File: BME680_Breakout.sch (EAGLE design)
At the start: 23 parts, among them U1 BME680, U4 PCA9515ADP, U8 LD1117XX

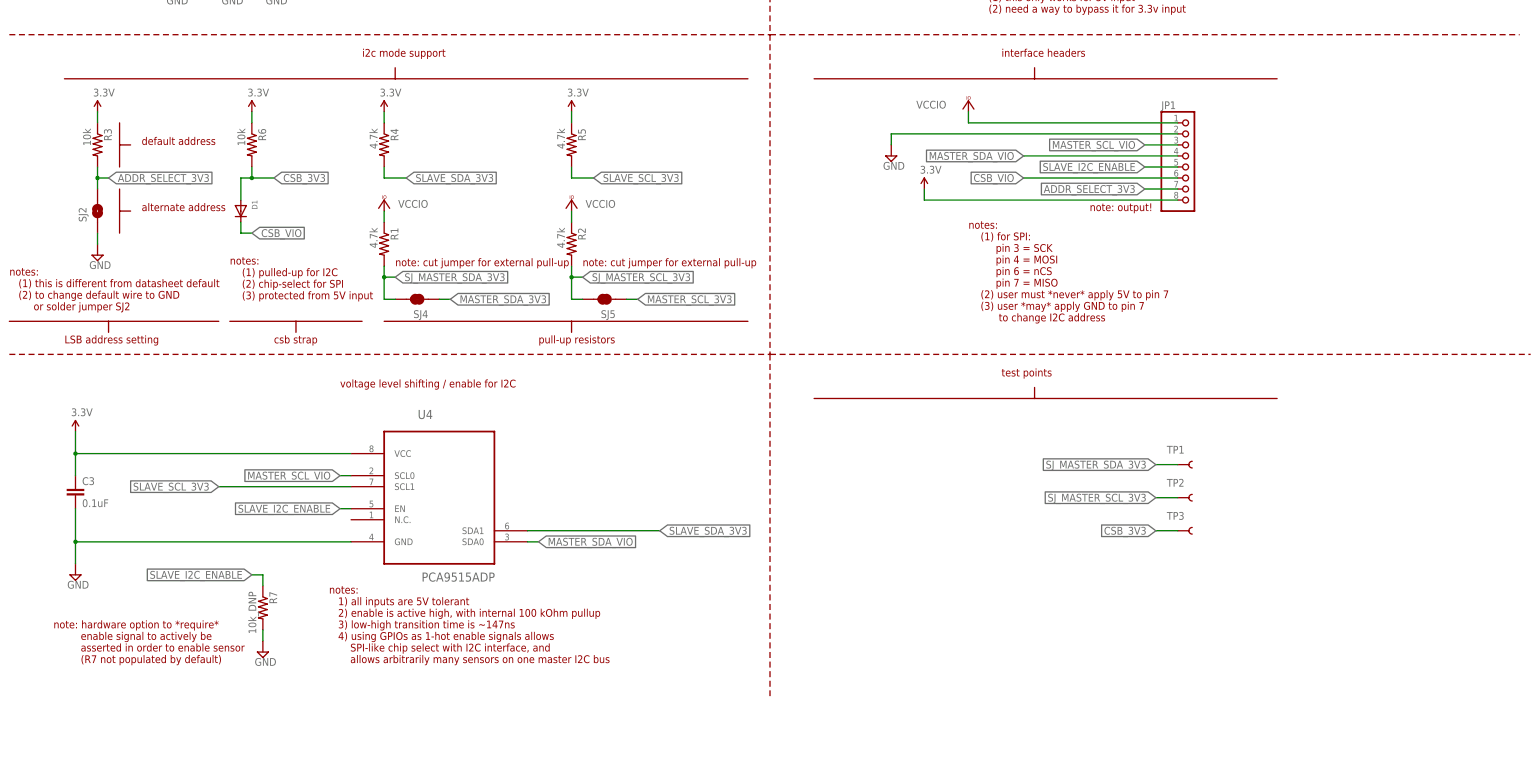
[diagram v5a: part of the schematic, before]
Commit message: asded zener diode and ptc fuse to address select input
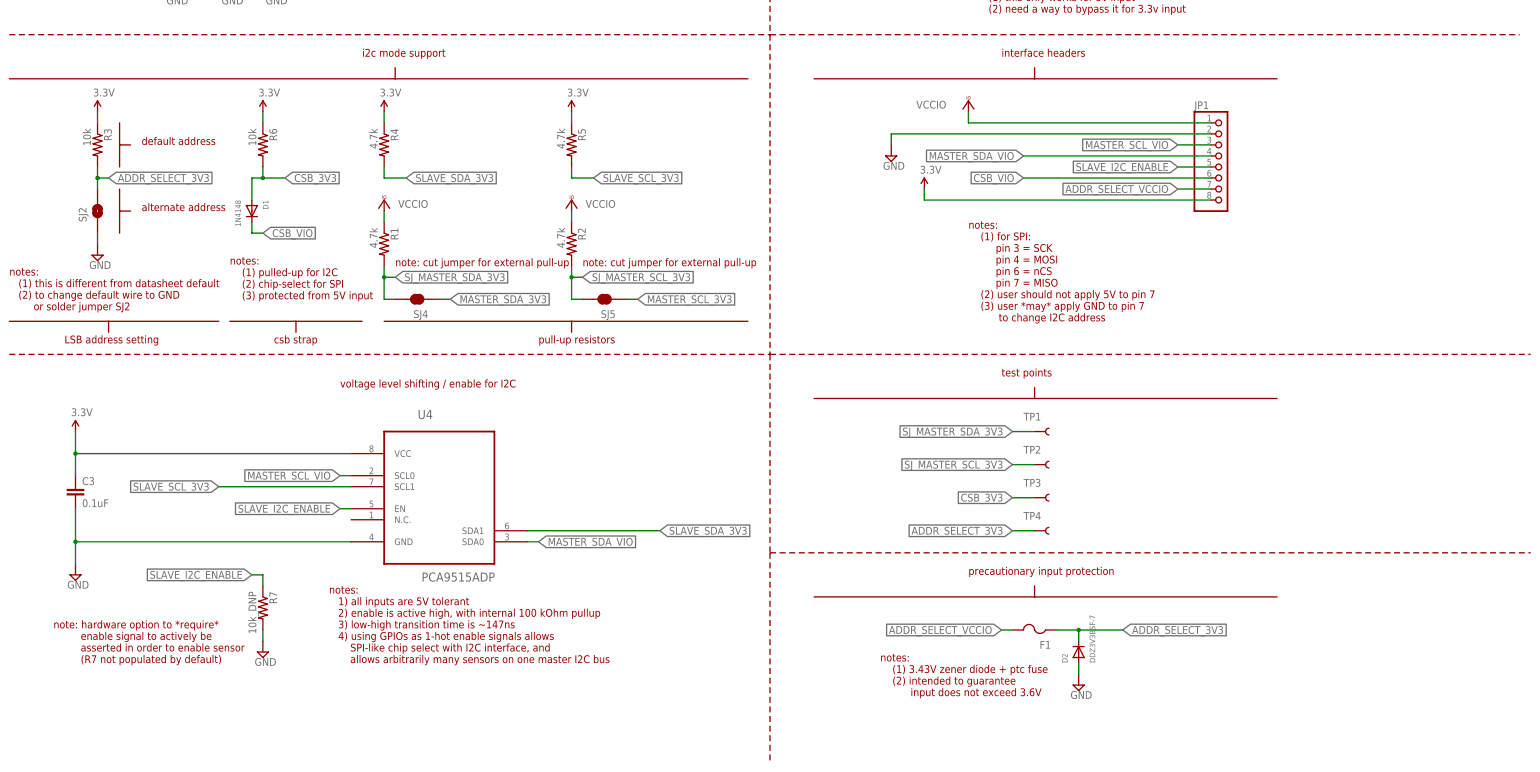
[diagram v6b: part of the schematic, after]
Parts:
- added D2: DDZ3V3BSF-7, adafruit:DIODESOD-323F
- added F1: (no value), adafruit:PTCFUSE-1812
- added TP4: TEST-POINT3X4, SparkFun-Passives:TEST-POINT3X4
- D1: value (none) -> 1N4148
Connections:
- new net ADDR_SELECT_VCCIO: F1.2, JP1.7
- net ADDR_SELECT_3V3: now also D2.C, F1.1, TP4.1; no longer JP1.7
- net GND: now also D2.A
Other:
- note added: "notes: (1) 3.43V zener diode + ptc fuse (2) intended to guarantee input does not exceed 3.6V"
- note added: "notes: (1) for SPI: pin 3 = SCK pin 4 = MOSI pin 6 = nCS pin 7 = MISO (2) user should not apply 5V to pin 7 (3) user *may* apply GND to pin 7 to change I2C address"
- note added: "precautionary input protection"
- note removed: "note: output!"
- note removed: "notes: (1) for SPI: pin 3 = SCK pin 4 = MOSI pin 6 = nCS pin 7 = MISO (2) user must *never* apply 5V to pin 7 (3) user *may* apply GND to pin 7 to change I2C address"
- moved on the sheet: D1, JP1, R6, TP1, TP2, TP3

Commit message: initial routing of PCB
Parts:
- added SJ1: JUMPER-PAD-2-NC_BY_TRACE, SparkFun-Passives:JUMPER-PAD-2-NC_BY_TRACE
- added SJ3: SOLDERJUMPERNC2, SparkFun-Retired:SOLDERJUMPERNC2
- added STANDOFF1, STANDOFF2, STANDOFF3, STANDOFF4: STAND-OFF, SparkFun-Electromechanical:STAND-OFF
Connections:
- net SJ_MASTER_SCL_3V3 renamed SJ_MASTER_SCL_VIO
- net SJ_MASTER_SDA_3V3 renamed SJ_MASTER_SDA_VIO
- removed net MASTER_SCL_3V3: SJ5.1
- removed net MASTER_SDA_3V3: SJ4.1
- new net N$1: SJ1.2, U8.VO
- net 3.3V: now also SJ1.1, SJ3.2; no longer U8.VO
- net MASTER_SCL_VIO: now also JP1.5, SJ5.1; no longer JP1.3
- net MASTER_SDA_VIO: now also SJ4.1
- net SLAVE_I2C_ENABLE: now also JP1.3; no longer JP1.5
- net VCCIO: now also SJ3.1
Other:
- note added: "notes: (1) for VCCIO = 5 default jumpers (2) for VCCIO = 3.3V bridge SJ3 and cut SJ1"
- note removed: "notes: (1) this only works for 5v input (2) need a way to bypass it for 3.3v input"
- moved on the sheet: C4, C5, R6, U8

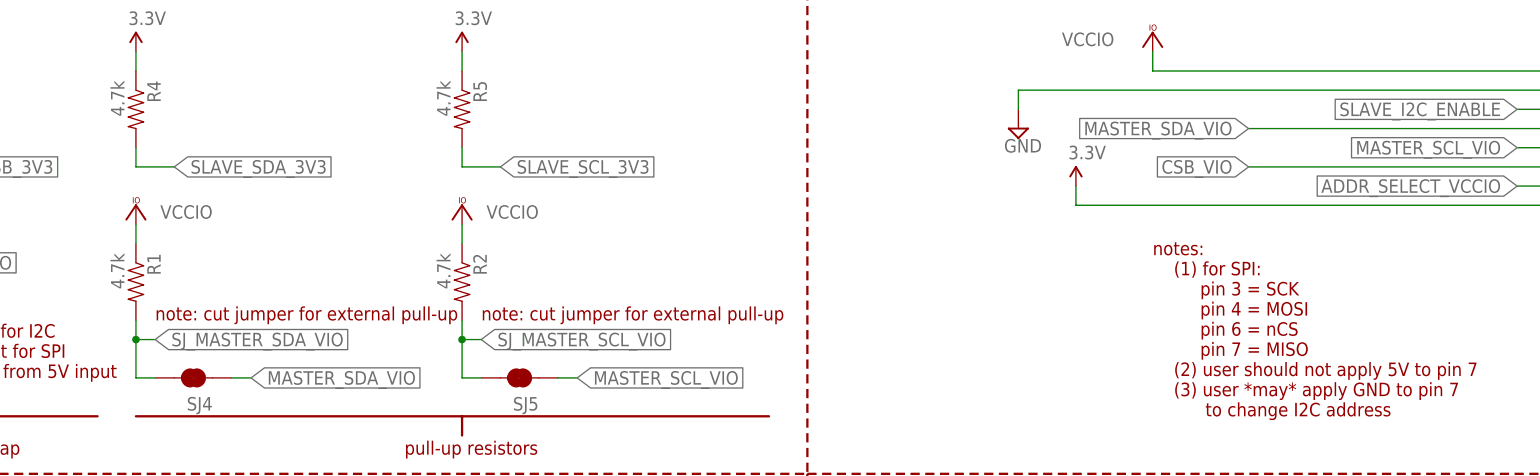
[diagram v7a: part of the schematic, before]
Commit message: added silk screen to back side; added to solder jumpers; minor routing changes
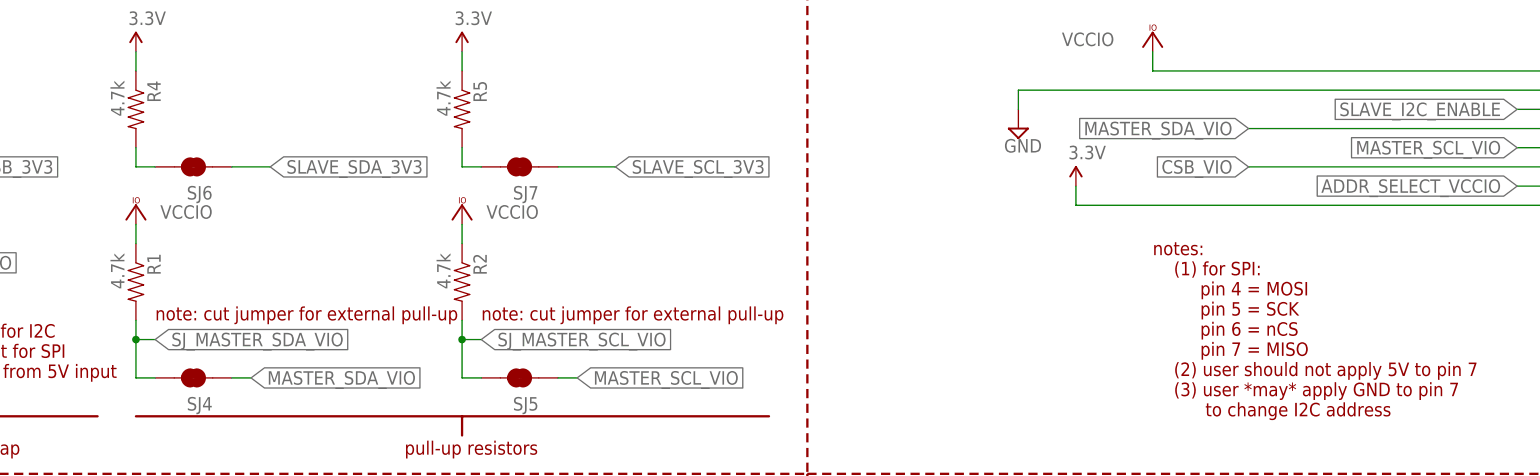
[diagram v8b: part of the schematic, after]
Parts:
- added SJ6, SJ7: JUMPER-PAD-2-NC_BY_TRACE, SparkFun-Passives:JUMPER-PAD-2-NC_BY_TRACE
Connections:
- new net N$3: R4.2, SJ6.2
- new net N$4: R5.2, SJ7.2
- net SLAVE_SCL_3V3: now also SJ7.1; no longer R5.2
- net SLAVE_SDA_3V3: now also SJ6.1; no longer R4.2
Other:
- note added: "notes: (1) for SPI: pin 4 = MOSI pin 5 = SCK pin 6 = nCS pin 7 = MISO (2) user should not apply 5V to pin 7 (3) user *may* apply GND to pin 7 to change I2C address"
- note removed: "notes: (1) for SPI: pin 3 = SCK pin 4 = MOSI pin 6 = nCS pin 7 = MISO (2) user should not apply 5V to pin 7 (3) user *may* apply GND to pin 7 to change I2C address"
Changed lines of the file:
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@@
 <part name="SJ1" library="SparkFun-Passives" deviceset="JUMPER-PAD-2-NC_BY_TRACE" device=""/>
 <part name="SJ3" library="SparkFun-Retired" deviceset="SOLDERJUMPER" device="NC2"/>
+<part name="SJ6" library="SparkFun-Passives" deviceset="JUMPER-PAD-2-NC_BY_TRACE" device=""/>
+<part name="SJ7" library="SparkFun-Passives" deviceset="JUMPER-PAD-2-NC_BY_TRACE" device=""/>
 </parts>
 <sheets>
@@
 <text x="264.16" y="121.92" size="1.778" layer="94">notes:
     (1) for SPI:
-         pin 3 = SCK
          pin 4 = MOSI
+         pin 5 = SCK
          pin 6 = nCS
          pin 7 = MISO
@@
 <attribute name="NAME" x="279.4" y="231.14" size="1.778" layer="95"/>
 </instance>
+<instance part="SJ6" gate="G$1" x="137.16" y="154.94" smashed="yes" rot="R180">
+<attribute name="NAME" x="139.7" y="152.4" size="1.778" layer="95" rot="R180"/>
+</instance>
+<instance part="SJ7" gate="G$1" x="180.34" y="154.94" smashed="yes" rot="R180">
+<attribute name="NAME" x="182.88" y="152.4" size="1.778" layer="95" rot="R180"/>
+</instance>
 </instances>
 <busses>
@@
 </segment>
 <segment>
-<pinref part="R5" gate="G$1" pin="2"/>
-<wire x1="172.72" y1="157.48" x2="172.72" y2="154.94" width="0.1524" layer="91"/>
-<wire x1="172.72" y1="154.94" x2="177.8" y2="154.94" width="0.1524" layer="91"/>
-<label x="177.8" y="154.94" size="1.778" layer="95" xref="yes"/>
+<label x="193.04" y="154.94" size="1.778" layer="95" xref="yes"/>
+<pinref part="SJ7" gate="G$1" pin="1"/>
+<wire x1="185.42" y1="154.94" x2="193.04" y2="154.94" width="0.1524" layer="91"/>
 </segment>
 <segment>
@@
 </segment>
 <segment>
-<pinref part="R4" gate="G$1" pin="2"/>
-<wire x1="129.54" y1="157.48" x2="129.54" y2="154.94" width="0.1524" layer="91"/>
-<wire x1="129.54" y1="154.94" x2="134.62" y2="154.94" width="0.1524" layer="91"/>
-<label x="134.62" y="154.94" size="1.778" layer="95" xref="yes"/>
+<label x="147.32" y="154.94" size="1.778" layer="95" xref="yes"/>
+<pinref part="SJ6" gate="G$1" pin="1"/>
+<wire x1="142.24" y1="154.94" x2="147.32" y2="154.94" width="0.1524" layer="91"/>
 </segment>
 </net>
@@
 </segment>
 </net>
+<net name="N$3" class="0">
+<segment>
+<pinref part="SJ6" gate="G$1" pin="2"/>
+<pinref part="R4" gate="G$1" pin="2"/>
+<wire x1="129.54" y1="157.48" x2="129.54" y2="154.94" width="0.1524" layer="91"/>
+<wire x1="129.54" y1="154.94" x2="132.08" y2="154.94" width="0.1524" layer="91"/>
+</segment>
+</net>
+<net name="N$4" class="0">
+<segment>
+<pinref part="SJ7" gate="G$1" pin="2"/>
+<pinref part="R5" gate="G$1" pin="2"/>
+<wire x1="172.72" y1="157.48" x2="172.72" y2="154.94" width="0.1524" layer="91"/>
+<wire x1="172.72" y1="154.94" x2="175.26" y2="154.94" width="0.1524" layer="91"/>
+</segment>
+</net>
